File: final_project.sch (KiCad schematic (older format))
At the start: 3 parts, among them J1 Conn_01x02_Female

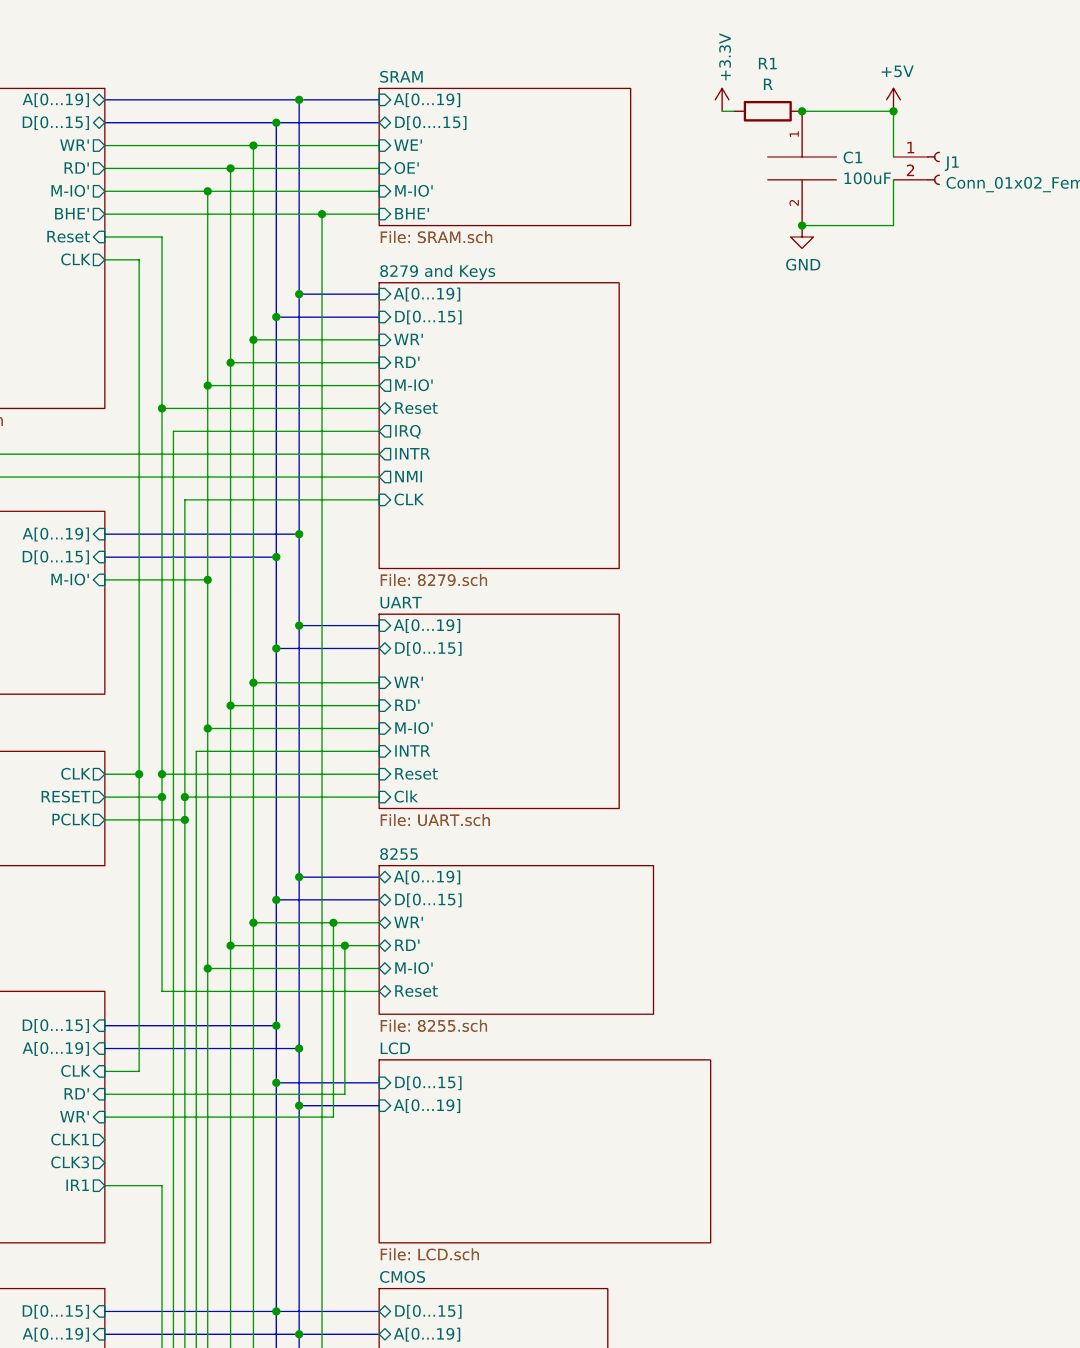
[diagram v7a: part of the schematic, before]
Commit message: LCD fixed
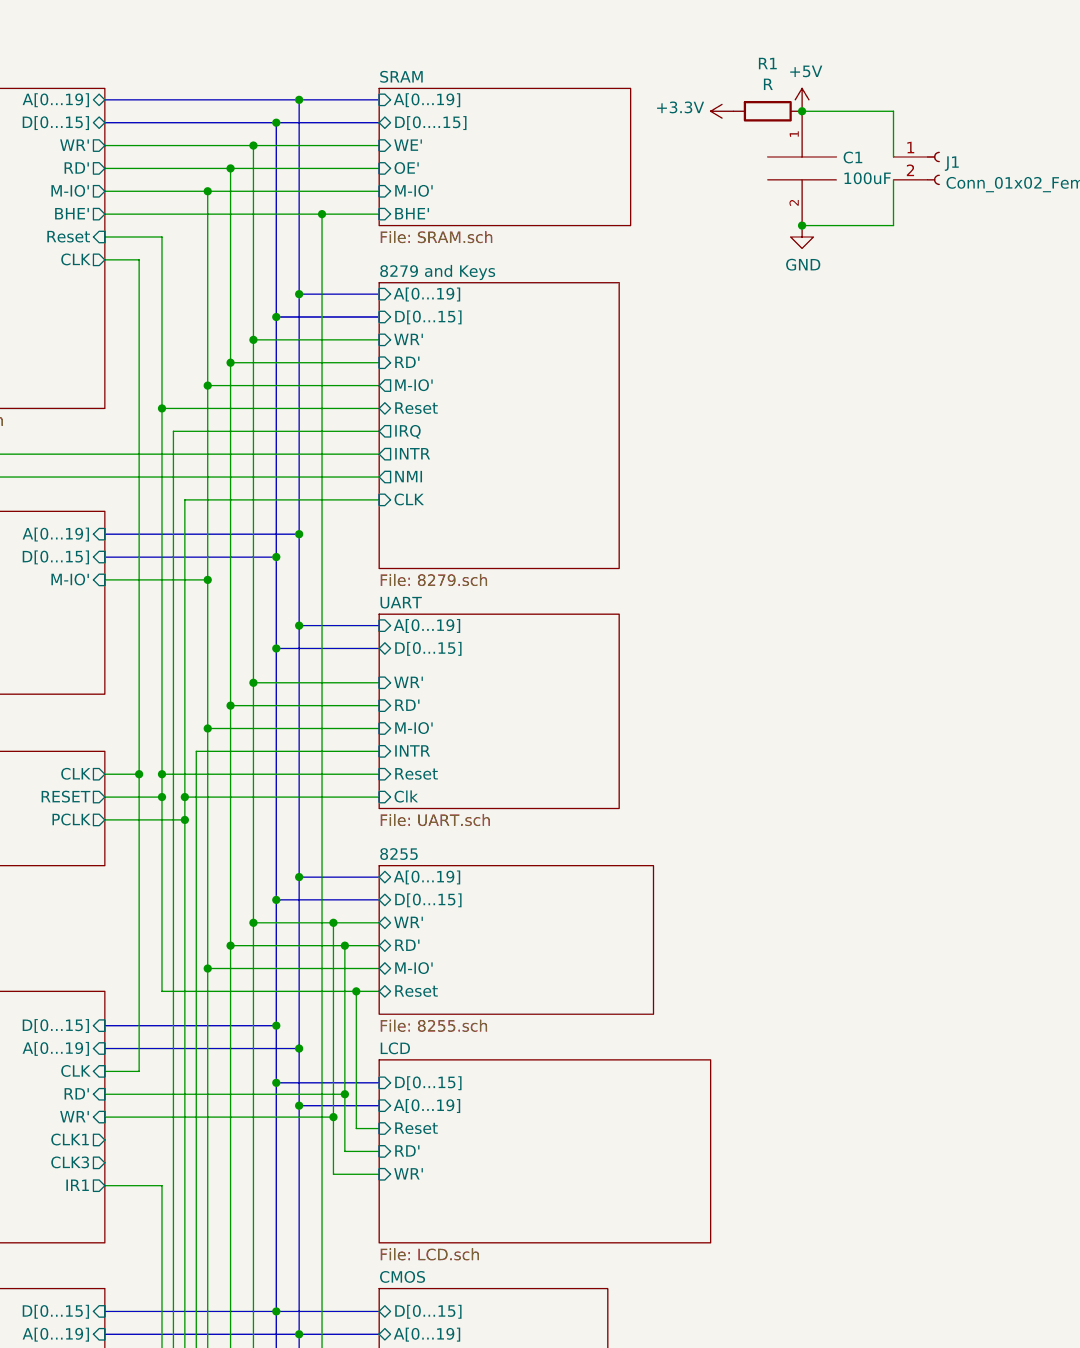
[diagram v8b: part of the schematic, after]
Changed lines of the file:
@@
 L power:+5V #PWR02
 U 1 1 625BB5A4
-P 6650 950
-F 0 "#PWR02" H 6650 800 50  0001 C CNN
-F 1 "+5V" H 6665 1123 50  0000 C CNN
-F 2 "" H 6650 950 50  0001 C CNN
-F 3 "" H 6650 950 50  0001 C CNN
-	1    6650 950
+P 6250 950
+F 0 "#PWR02" H 6250 800 50  0001 C CNN
+F 1 "+5V" H 6265 1123 50  0000 C CNN
+F 2 "" H 6250 950 50  0001 C CNN
+F 3 "" H 6250 950 50  0001 C CNN
+	1    6250 950
 	1    0    0    -1
 $EndComp
@@
 F2 "D[0...15]" I L 4400 5200 50
 F3 "A[0...19]" I L 4400 5300 50
+F4 "Reset" I L 4400 5400 50
+F5 "RD'" I L 4400 5500 50
+F6 "WR'" I L 4400 5600 50
 $EndSheet
 $Sheet
@@
 L power:+3.3V #PWR01
 U 1 1 630D8F6E
-P 5900 950
-F 0 "#PWR01" H 5900 800 50  0001 C CNN
-F 1 "+3.3V" V 5915 1078 50  0000 L CNN
-F 2 "" H 5900 950 50  0001 C CNN
-F 3 "" H 5900 950 50  0001 C CNN
-	1    5900 950
-	1    0    0    -1
+P 5950 950
+F 0 "#PWR01" H 5950 800 50  0001 C CNN
+F 1 "+3.3V" V 5965 1078 50  0000 L CNN
+F 2 "" H 5950 950 50  0001 C CNN
+F 3 "" H 5950 950 50  0001 C CNN
+	1    5950 950
+	0    -1   -1   0
 $EndComp
 Wire Wire Line
 	4200 4500 4200 5350
 Wire Wire Line
-	3450 4800 4400 4800
+	3450 4800 4300 4800
 Connection ~ 3950 5200
 Wire Bus Line
@@
 Wire Bus Line
 	4050 5050 4050 5300
-Connection ~ 6650 950
-Wire Wire Line
-	5950 950  5900 950
+Wire Wire Line
+	4250 5250 4250 5500
+Wire Wire Line
+	4250 5500 4400 5500
+Connection ~ 4250 5250
+Wire Wire Line
+	4400 5400 4300 5400
+Wire Wire Line
+	4300 5400 4300 4800
+Connection ~ 4300 4800
+Wire Wire Line
+	4300 4800 4400 4800
+Wire Wire Line
+	4200 5350 4200 5600
+Wire Wire Line
+	4200 5600 4400 5600
+Connection ~ 4200 5350
 $EndSCHEMATC
